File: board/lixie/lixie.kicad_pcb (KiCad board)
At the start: 2 copper layers, 1 part

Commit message: made some footprints, fixed the power diode circuitry
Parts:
- removed REF**: QFP_64, lixie:STM32L073RZT3
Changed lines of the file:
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@@
     (tracks 0)
     (zones 0)
-    (modules 1)
+    (modules 0)
     (nets 1)
   )
@@
     (uvia_drill 0.1)
   )
-  (module lixie:STM32L073RZT3 (layer F.Cu)
-    (at 154.3 95.3)
-    (fp_text reference REF** (at 0 -7.55) (layer F.SilkS)
-      (effects (font (size 1.2 1.2) (thickness 0.15)))
-    )
-    (fp_text value QFP_64 (at 0 7.55) (layer F.Fab)
-      (effects (font (size 1.2 1.2) (thickness 0.15)))
-    )
-    (fp_line (start -5 -4.25) (end -4.25 -5) (layer F.SilkS) (width 0.15))
-    (fp_line (start 4.25 -5) (end 5 -5) (layer F.SilkS) (width 0.15))
-    (fp_line (start 5 -5) (end 5 -4.25) (layer F.SilkS) (width 0.15))
-    (fp_line (start -4.25 5) (end -5 5) (layer F.SilkS) (width 0.15))
-    (fp_line (start -5 5) (end -5 4.25) (layer F.SilkS) (width 0.15))
-    (fp_line (start 4.25 5) (end 5 5) (layer F.SilkS) (width 0.15))
-    (fp_line (start 5 5) (end 5 4.25) (layer F.SilkS) (width 0.15))
-    (fp_line (start -6.6 -6.6) (end 6.6 -6.6) (layer F.CrtYd) (width 0.15))
-    (fp_line (start 6.6 -6.6) (end 6.6 6.6) (layer F.CrtYd) (width 0.15))
-    (fp_line (start 6.6 6.6) (end -6.6 6.6) (layer F.CrtYd) (width 0.15))
-    (fp_line (start -6.6 6.6) (end -6.6 -6.6) (layer F.CrtYd) (width 0.15))
-    (pad 1 smd oval (at -5.75 -3.75 90) (size 0.3 1.2) (layers F.Cu F.Paste F.Mask)
-      (solder_mask_margin 0.001))
-    (pad 2 smd oval (at -5.75 -3.25 90) (size 0.3 1.2) (layers F.Cu F.Paste F.Mask)
-      (solder_mask_margin 0.0001))
-    (pad 3 smd oval (at -5.75 -2.75 90) (size 0.3 1.2) (layers F.Cu F.Paste F.Mask)
-      (solder_mask_margin 0.000001))
-    (pad 4 smd oval (at -5.75 -2.25 90) (size 0.3 1.2) (layers F.Cu F.Paste F.Mask)
-      (solder_mask_margin 0.000001))
-    (pad 5 smd oval (at -5.75 -1.75 90) (size 0.3 1.2) (layers F.Cu F.Paste F.Mask)
-      (solder_mask_margin 0.000001))
-    (pad 6 smd oval (at -5.75 -1.25 90) (size 0.3 1.2) (layers F.Cu F.Paste F.Mask)
-      (solder_mask_margin 0.000001))
-    (pad 7 smd oval (at -5.75 -0.75 90) (size 0.3 1.2) (layers F.Cu F.Paste F.Mask)
-      (solder_mask_margin 0.000001))
-    (pad 8 smd oval (at -5.75 -0.25 90) (size 0.3 1.2) (layers F.Cu F.Paste F.Mask)
-      (solder_mask_margin 0.000001))
-    (pad 9 smd oval (at -5.75 0.25 90) (size 0.3 1.2) (layers F.Cu F.Paste F.Mask)
-      (solder_mask_margin 0.000001))
-    (pad 10 smd oval (at -5.75 0.75 270) (size 0.3 1.2) (layers F.Cu F.Paste F.Mask)
-      (solder_mask_margin 0.000001))
-    (pad 11 smd oval (at -5.75 1.25 270) (size 0.3 1.2) (layers F.Cu F.Paste F.Mask)
-      (solder_mask_margin 0.000001))
-    (pad 12 smd oval (at -5.75 1.75 90) (size 0.3 1.2) (layers F.Cu F.Paste F.Mask)
-      (solder_mask_margin 0.000001))
-    (pad 13 smd oval (at -5.75 2.25 270) (size 0.3 1.2) (layers F.Cu F.Paste F.Mask)
-      (solder_mask_margin 0.000001))
-    (pad 14 smd oval (at -5.75 2.75 90) (size 0.3 1.2) (layers F.Cu F.Paste F.Mask)
-      (solder_mask_margin 0.000001))
-    (pad 15 smd oval (at -5.75 3.25 90) (size 0.3 1.2) (layers F.Cu F.Paste F.Mask)
-      (solder_mask_margin 0.000001))
-    (pad 16 smd oval (at -5.75 3.75 90) (size 0.3 1.2) (layers F.Cu F.Paste F.Mask)
-      (solder_mask_margin 0.000001))
-    (pad 17 smd oval (at -3.75 5.75) (size 0.3 1.2) (layers F.Cu F.Paste F.Mask)
-      (solder_mask_margin 0.000001))
-    (pad 18 smd oval (at -3.25 5.75) (size 0.3 1.2) (layers F.Cu F.Paste F.Mask)
-      (solder_mask_margin 0.000001))
-    (pad 19 smd oval (at -2.75 5.75) (size 0.3 1.2) (layers F.Cu F.Paste F.Mask)
-      (solder_mask_margin 0.000001))
-    (pad 20 smd oval (at -2.25 5.75) (size 0.3 1.2) (layers F.Cu F.Paste F.Mask)
-      (solder_mask_margin 0.000001))
-    (pad 21 smd oval (at -1.75 5.75) (size 0.3 1.2) (layers F.Cu F.Paste F.Mask)
-      (solder_mask_margin 0.000001))
-    (pad 22 smd oval (at -1.25 5.75) (size 0.3 1.2) (layers F.Cu F.Paste F.Mask)
-      (solder_mask_margin 0.000001))
-    (pad 23 smd oval (at -0.75 5.75) (size 0.3 1.2) (layers F.Cu F.Paste F.Mask)
-      (solder_mask_margin 0.000001))
-    (pad 24 smd oval (at -0.25 5.75) (size 0.3 1.2) (layers F.Cu F.Paste F.Mask)
-      (solder_mask_margin 0.000001))
-    (pad 25 smd oval (at 0.25 5.75) (size 0.3 1.2) (layers F.Cu F.Paste F.Mask)
-      (solder_mask_margin 0.000001))
-    (pad 26 smd oval (at 0.75 5.75) (size 0.3 1.2) (layers F.Cu F.Paste F.Mask)
-      (solder_mask_margin 0.000001))
-    (pad 27 smd oval (at 1.25 5.75) (size 0.3 1.2) (layers F.Cu F.Paste F.Mask)
-      (solder_mask_margin 0.000001))
-    (pad 28 smd oval (at 1.75 5.75) (size 0.3 1.2) (layers F.Cu F.Paste F.Mask)
-      (solder_mask_margin 0.000001))
-    (pad 29 smd oval (at 2.25 5.75) (size 0.3 1.2) (layers F.Cu F.Paste F.Mask)
-      (solder_mask_margin 0.000001))
-    (pad 30 smd oval (at 2.75 5.75) (size 0.3 1.2) (layers F.Cu F.Paste F.Mask)
-      (solder_mask_margin 0.000001))
-    (pad 31 smd oval (at 3.25 5.75) (size 0.3 1.2) (layers F.Cu F.Paste F.Mask)
-      (solder_mask_margin 0.000001))
-    (pad 32 smd oval (at 3.75 5.75) (size 0.3 1.2) (layers F.Cu F.Paste F.Mask)
-      (solder_mask_margin 0.000001))
-    (pad 33 smd oval (at 5.75 3.75 90) (size 0.3 1.2) (layers F.Cu F.Paste F.Mask)
-      (solder_mask_margin 0.000001))
-    (pad 34 smd oval (at 5.75 3.25 90) (size 0.3 1.2) (layers F.Cu F.Paste F.Mask)
-      (solder_mask_margin 0.000001))
-    (pad 35 smd oval (at 5.75 2.75 90) (size 0.3 1.2) (layers F.Cu F.Paste F.Mask)
-      (solder_mask_margin 0.000001))
-    (pad 36 smd oval (at 5.75 2.25 90) (size 0.3 1.2) (layers F.Cu F.Paste F.Mask)
-      (solder_mask_margin 0.000001))
-    (pad 37 smd oval (at 5.75 1.75 90) (size 0.3 1.2) (layers F.Cu F.Paste F.Mask)
-      (solder_mask_margin 0.000001))
-    (pad 38 smd oval (at 5.75 1.25 90) (size 0.3 1.2) (layers F.Cu F.Paste F.Mask)
-      (solder_mask_margin 0.000001))
-    (pad 39 smd oval (at 5.75 0.75 90) (size 0.3 1.2) (layers F.Cu F.Paste F.Mask)
-      (solder_mask_margin 0.000001))
-    (pad 40 smd oval (at 5.75 0.25 90) (size 0.3 1.2) (layers F.Cu F.Paste F.Mask)
-      (solder_mask_margin 0.000001))
-    (pad 41 smd oval (at 5.75 -0.25 90) (size 0.3 1.2) (layers F.Cu F.Paste F.Mask)
-      (solder_mask_margin 0.000001))
-    (pad 42 smd oval (at 5.75 -0.75 90) (size 0.3 1.2) (layers F.Cu F.Paste F.Mask)
-      (solder_mask_margin 0.000001))
-    (pad 43 smd oval (at 5.75 -1.25 90) (size 0.3 1.2) (layers F.Cu F.Paste F.Mask)
-      (solder_mask_margin 0.000001))
-    (pad 44 smd oval (at 5.75 -1.75 90) (size 0.3 1.2) (layers F.Cu F.Paste F.Mask)
-      (solder_mask_margin 0.000001))
-    (pad 45 smd oval (at 5.75 -2.25 90) (size 0.3 1.2) (layers F.Cu F.Paste F.Mask)
-      (solder_mask_margin 0.000001))
-    (pad 46 smd oval (at 5.75 -2.75 90) (size 0.3 1.2) (layers F.Cu F.Paste F.Mask)
-      (solder_mask_margin 0.000001))
-    (pad 47 smd oval (at 5.75 -3.25 90) (size 0.3 1.2) (layers F.Cu F.Paste F.Mask)
-      (solder_mask_margin 0.000001))
-    (pad 48 smd oval (at 5.75 -3.75 90) (size 0.3 1.2) (layers F.Cu F.Paste F.Mask)
-      (solder_mask_margin 0.000001))
-    (pad 49 smd oval (at 3.75 -5.75) (size 0.3 1.2) (layers F.Cu F.Paste F.Mask)
-      (solder_mask_margin 0.000001))
-    (pad 50 smd oval (at 3.25 -5.75) (size 0.3 1.2) (layers F.Cu F.Paste F.Mask)
-      (solder_mask_margin 0.000001))
-    (pad 51 smd oval (at 2.75 -5.75) (size 0.3 1.2) (layers F.Cu F.Paste F.Mask)
-      (solder_mask_margin 0.000001))
-    (pad 52 smd oval (at 2.25 -5.75) (size 0.3 1.2) (layers F.Cu F.Paste F.Mask)
-      (solder_mask_margin 0.000001))
-    (pad 53 smd oval (at 1.75 -5.75) (size 0.3 1.2) (layers F.Cu F.Paste F.Mask)
-      (solder_mask_margin 0.000001))
-    (pad 54 smd oval (at 1.25 -5.75) (size 0.3 1.2) (layers F.Cu F.Paste F.Mask)
-      (solder_mask_margin 0.000001))
-    (pad 55 smd oval (at 0.75 -5.75) (size 0.3 1.2) (layers F.Cu F.Paste F.Mask)
-      (solder_mask_margin 0.000001))
-    (pad 56 smd oval (at 0.25 -5.75) (size 0.3 1.2) (layers F.Cu F.Paste F.Mask)
-      (solder_mask_margin 0.000001))
-    (pad 57 smd oval (at -0.25 -5.75) (size 0.3 1.2) (layers F.Cu F.Paste F.Mask)
-      (solder_mask_margin 0.000001))
-    (pad 58 smd oval (at -0.75 -5.75) (size 0.3 1.2) (layers F.Cu F.Paste F.Mask)
-      (solder_mask_margin 0.000001))
-    (pad 59 smd oval (at -1.25 -5.75) (size 0.3 1.2) (layers F.Cu F.Paste F.Mask)
-      (solder_mask_margin 0.000001))
-    (pad 60 smd oval (at -1.75 -5.75) (size 0.3 1.2) (layers F.Cu F.Paste F.Mask)
-      (solder_mask_margin 0.000001))
-    (pad 61 smd oval (at -2.25 -5.75) (size 0.3 1.2) (layers F.Cu F.Paste F.Mask)
-      (solder_mask_margin 0.000001))
-    (pad 62 smd oval (at -2.75 -5.75) (size 0.3 1.2) (layers F.Cu F.Paste F.Mask)
-      (solder_mask_margin 0.000001))
-    (pad 63 smd oval (at -3.25 -5.75) (size 0.3 1.2) (layers F.Cu F.Paste F.Mask)
-      (solder_mask_margin 0.000001))
-    (pad 64 smd oval (at -3.75 -5.75) (size 0.3 1.2) (layers F.Cu F.Paste F.Mask)
-      (solder_mask_margin 0.000001))
-  )
 )

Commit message: started working on layout
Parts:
- added BT1: Battery_Cell, Pin_Headers:Pin_Header_Straight_1x02, F.Cu at (82.0, 75.5)
- added D1: LED_ARGB, lixie:LED_ARGB_0606, F.Cu at (93.0, 89.0)
- added D10: LED_ARGB, lixie:LED_ARGB_0606, F.Cu at (103.0, 83.0)
- added D11: LED_ARGB, lixie:LED_ARGB_0606, F.Cu at (113.0, 83.0)
- added D12: LED_ARGB, lixie:LED_ARGB_0606, F.Cu at (123.0, 83.0)
- added D13: LED_ARGB, lixie:LED_ARGB_0606, F.Cu at (98.0, 80.0)
- added D14: LED_ARGB, lixie:LED_ARGB_0606, F.Cu at (108.0, 80.0)
- added D15: LED_ARGB, lixie:LED_ARGB_0606, F.Cu at (118.2, 80.0)
- added D16: LED_ARGB, lixie:LED_ARGB_0606, F.Cu at (128.0, 80.0)
- added D17: D, Diodes_SMD:SOD-123, F.Cu at (85.8, 62.0)
- added D2: LED_ARGB, lixie:LED_ARGB_0606, F.Cu at (103.0, 89.0)
- added D3: LED_ARGB, lixie:LED_ARGB_0606, F.Cu at (113.0, 89.0)
- added D4: LED_ARGB, lixie:LED_ARGB_0606, F.Cu at (123.0, 89.0)
- added D5: LED_ARGB, lixie:LED_ARGB_0606, F.Cu at (98.0, 86.0)
- added D6: LED_ARGB, lixie:LED_ARGB_0606, F.Cu at (108.0, 86.0)
- added D7: LED_ARGB, lixie:LED_ARGB_0606, F.Cu at (118.2, 86.0)
- added D8: LED_ARGB, lixie:LED_ARGB_0606, F.Cu at (128.0, 86.0)
- added D9: LED_ARGB, lixie:LED_ARGB_0606, F.Cu at (93.0, 83.0)
- added LS1: Speaker, lixie:PKMCS0909E4000-R1, F.Cu at (111.5, 63.8)
- added P1: USB_OTG, lixie:USB_Micro-B_Molex-105017-0001, F.Cu at (142.0, 73.0)
- added R1: 100k, Resistors_SMD:R_0805_HandSoldering, F.Cu at (87.0, 67.5)
- added R2: 100k, Resistors_SMD:R_0805_HandSoldering, F.Cu at (90.0, 67.5)
- added R3: 100k, Resistors_SMD:R_0805_HandSoldering, F.Cu at (93.0, 67.5)
- added R4: 10k, Resistors_SMD:R_0805_HandSoldering, F.Cu at (136.8, 62.8)
- added R5: R, Resistors_SMD:R_0805_HandSoldering, F.Cu at (136.7, 68.8)
- added U1: IS31FL3738, lixie:IS31FL3738, F.Cu at (101.0, 66.2)
- added U2: MIC550x, lixie:MIC550x, F.Cu at (95.2, 61.8)
- added U3: MAX40200, lixie:MAX40200, F.Cu at (90.0, 61.8)
- added U4: STM32L073xZ, lixie:STM32L073RZT3, F.Cu at (127.8, 65.8)
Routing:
- net Net-(D10-Pad2): track 0.00 -> 60.6 mm, vias 0 -> 8
- net Net-(D10-Pad4): track 0.00 -> 53.7 mm
- net Net-(D1-Pad4): track 0.00 -> 49.5 mm
- net Net-(D1-Pad3): track 0.00 -> 47.9 mm
- net Net-(D10-Pad3): track 0.00 -> 46.0 mm
- net Net-(D1-Pad2): track 0.00 -> 37.5 mm, vias 0 -> 5
- net VBUS: track 0.00 -> 14.4 mm
- net Net-(D7-Pad2): track 0.00 -> 12.0 mm, vias 0 -> 2
- net Net-(D12-Pad1): track 0.00 -> 6.82 mm, vias 0 -> 2
- net Net-(D16-Pad1): track 0.00 -> 6.82 mm, vias 0 -> 2
- net Net-(D14-Pad1): track 0.00 -> 6.82 mm, vias 0 -> 2
- net Net-(D13-Pad1): track 0.00 -> 6.82 mm, vias 0 -> 2
- net Net-(D1-Pad1): track 0.00 -> 6.75 mm, vias 0 -> 2
- net Net-(D11-Pad1): track 0.00 -> 6.68 mm, vias 0 -> 2
- net Net-(D15-Pad1): track 0.00 -> 6.59 mm, vias 0 -> 2
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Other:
- board outline added: 67.5 x 37.8 mm

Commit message: laid out the board
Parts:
- removed LS1: Speaker, lixie:PKMCS0909E4000-R1
- added F1: Polyfuse, Resistors_SMD:R_1206_HandSoldering, F.Cu at (74.2, 77.3)
- added F2: Polyfuse, Resistors_SMD:R_1206_HandSoldering, F.Cu at (84.3, 75.4)
- added F3: Polyfuse, Resistors_SMD:R_1206_HandSoldering, F.Cu at (130.0, 73.0)
- added R6: 4.7k, Resistors_SMD:R_0805_HandSoldering, F.Cu at (102.2, 65.8)
- added SLEEP: SW_Push, Buttons_Switches_SMD:SW_SPST_TL3342, F.Cu at (80.6, 66.9)
- added SWD: CONN_01X04, Pin_Headers:Pin_Header_Straight_1x04, F.Cu at (119.8, 80.4)
- D1, D10, D11, D12, D13, D14, D15, D16, D2, D3, D4, D5, D6, D7, D8, D9: value LED_ARGB -> LED_RGAB
- R5: value R -> 4.7k
- moved R5 32.6 mm to (104.3, 65.8)
- moved D17 17.4 mm to (73.2, 74.0), turned to 180 degrees
- moved U3 16.8 mm to (78.2, 73.7), turned to 0 degrees
- moved U2 16.3 mm to (82.6, 72.1), turned to 90 degrees
- moved R3 11.9 mm to (103.7, 72.6)
- moved BT1 8.96 mm to (74.6, 80.6), turned to 270 degrees
- moved D1 8.06 mm to (86.0, 93.0)
- moved D10 8.06 mm to (96.0, 87.0)
- moved D11 8.06 mm to (106.0, 87.0)
- moved D12 8.06 mm to (116.0, 87.0)
- moved D13 8.06 mm to (91.0, 84.0)
- moved D14 8.06 mm to (101.0, 84.0)
- moved D15 8.06 mm to (111.2, 84.0)
- moved D16 8.06 mm to (121.0, 84.0)
- moved D2 8.06 mm to (96.0, 93.0)
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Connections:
- net Net-(R3-Pad1) renamed /LED_CURRENT
- D11 pad 1: Net-(D11-Pad1) -> Net-(D10-Pad1)
- D11 pad 3: Net-(D10-Pad3) -> Net-(D11-Pad3)
- D12 pad 1: Net-(D12-Pad1) -> Net-(D10-Pad1)
- D12 pad 3: Net-(D10-Pad3) -> Net-(D12-Pad3)
- D13 pad 1: Net-(D13-Pad1) -> Net-(D10-Pad1)
- D13 pad 3: Net-(D10-Pad3) -> Net-(D13-Pad3)
- D14 pad 1: Net-(D14-Pad1) -> Net-(D10-Pad1)
- D14 pad 3: Net-(D10-Pad3) -> Net-(D14-Pad3)
- D15 pad 1: Net-(D15-Pad1) -> Net-(D10-Pad1)
- D15 pad 3: Net-(D10-Pad3) -> Net-(D15-Pad3)
- D16 pad 1: Net-(D16-Pad1) -> Net-(D10-Pad1)
- D16 pad 3: Net-(D10-Pad3) -> Net-(D16-Pad3)
- D17 pad 1: VBUS -> Net-(D17-Pad1)
- D17 pad 2: +5V -> Net-(D17-Pad2)
- D2 pad 1: Net-(D10-Pad1) -> Net-(D1-Pad1)
- D2 pad 3: Net-(D1-Pad3) -> Net-(D10-Pad3)
- D3 pad 1: Net-(D11-Pad1) -> Net-(D1-Pad1)
- D3 pad 3: Net-(D1-Pad3) -> Net-(D11-Pad3)
- D4 pad 1: Net-(D12-Pad1) -> Net-(D1-Pad1)
- D4 pad 3: Net-(D1-Pad3) -> Net-(D12-Pad3)
- D5 pad 1: Net-(D13-Pad1) -> Net-(D1-Pad1)
- D5 pad 3: Net-(D1-Pad3) -> Net-(D13-Pad3)
- D6 pad 1: Net-(D14-Pad1) -> Net-(D1-Pad1)
- D6 pad 3: Net-(D1-Pad3) -> Net-(D14-Pad3)
- D7 pad 1: Net-(D15-Pad1) -> Net-(D1-Pad1)
- D7 pad 2: Net-(D7-Pad2) -> Net-(D1-Pad2)
- D7 pad 3: Net-(D1-Pad3) -> Net-(D15-Pad3)
- D8 pad 1: Net-(D16-Pad1) -> Net-(D1-Pad1)
- D8 pad 2: Net-(D7-Pad2) -> Net-(D1-Pad2)
- D8 pad 3: Net-(D1-Pad3) -> Net-(D16-Pad3)
- D9 pad 1: Net-(D1-Pad1) -> Net-(D10-Pad1)
- D9 pad 3: Net-(D10-Pad3) -> Net-(D1-Pad3)
- R5 pad 1: /PIEZO -> +3V3
- R5 pad 2: Net-(LS1-Pad2) -> /SDA
- U1 pad 10: Net-(D1-Pad1) -> Net-(D1-Pad3)
- U1 pad 11: Net-(D10-Pad1) -> Net-(D10-Pad3)
- U1 pad 13: Net-(D11-Pad1) -> Net-(D11-Pad3)
- U1 pad 14: Net-(D12-Pad1) -> Net-(D12-Pad3)
- U1 pad 15: Net-(D13-Pad1) -> Net-(D13-Pad3)
- U1 pad 16: Net-(D14-Pad1) -> Net-(D14-Pad3)
- U1 pad 18: Net-(D15-Pad1) -> Net-(D15-Pad3)
- U1 pad 19: Net-(D16-Pad1) -> Net-(D16-Pad3)
- U1 pad 3: Net-(D10-Pad3) -> Net-(D10-Pad2)
- U1 pad 5: Net-(D10-Pad2) -> Net-(D10-Pad1)
- U1 pad 7: Net-(D1-Pad3) -> Net-(D1-Pad2)
- U1 pad 9: Net-(D1-Pad2) -> Net-(D1-Pad1)
- U3 pad 1: +BATT -> Net-(F1-Pad1)
- U3 pad 3: +BATT -> Net-(F1-Pad1)
- U3 pad 5: VBUS -> Net-(D17-Pad1)
- U4 pad 2: /BTN_SLEEP -> Net-(SW1-Pad2)
- U4 pad 46: /DBG_TMS -> /SWDIO
- U4 pad 49: /DBG_TCK -> /SWCLK
- U4 pad 53: /PIEZO -> Net-(U4-Pad53)
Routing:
- net +3V3: track 0.00 -> 98.8 mm, vias 0 -> 2
- net Net-(D17-Pad2): track 0.00 -> 93.7 mm, vias 0 -> 2
- net Net-(D1-Pad1): track 6.75 -> 75.4 mm, vias 2 -> 0
- net Net-(D10-Pad1): track 6.59 -> 64.7 mm
- net GND: track 0.00 -> 57.9 mm, vias 0 -> 15
- net Net-(SW1-Pad2): track 0.00 -> 50.5 mm
- net Net-(D1-Pad2): track 37.5 -> 87.8 mm, vias 5 -> 12
- net Net-(D1-Pad4): track 49.5 -> 95.0 mm, vias 0 -> 2
- net VBUS: track 14.4 -> 57.0 mm, vias 0 -> 5
- net Net-(D10-Pad4): track 53.7 -> 95.3 mm, vias 0 -> 4
- net Net-(D16-Pad3): track 0.00 -> 39.1 mm, vias 0 -> 3
- net Net-(D12-Pad3): track 0.00 -> 35.4 mm, vias 0 -> 3
- net Net-(D15-Pad3): track 0.00 -> 35.0 mm, vias 0 -> 3
- net /SDA: track 0.00 -> 32.0 mm, vias 0 -> 2
- net /SCL: track 0.00 -> 30.8 mm, vias 0 -> 2
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- added copper zone on B.Cu, net GND
- added copper zone on F.Cu, net GND
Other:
- net class Default: clearance 0.2 -> 0.19999
- rule trace_clearance: 0.2 -> 0.19999
- board text added: "-"
- board text added: "CLK"
- board text added: "G"
- board text added: "IO"
- board text added: "V"

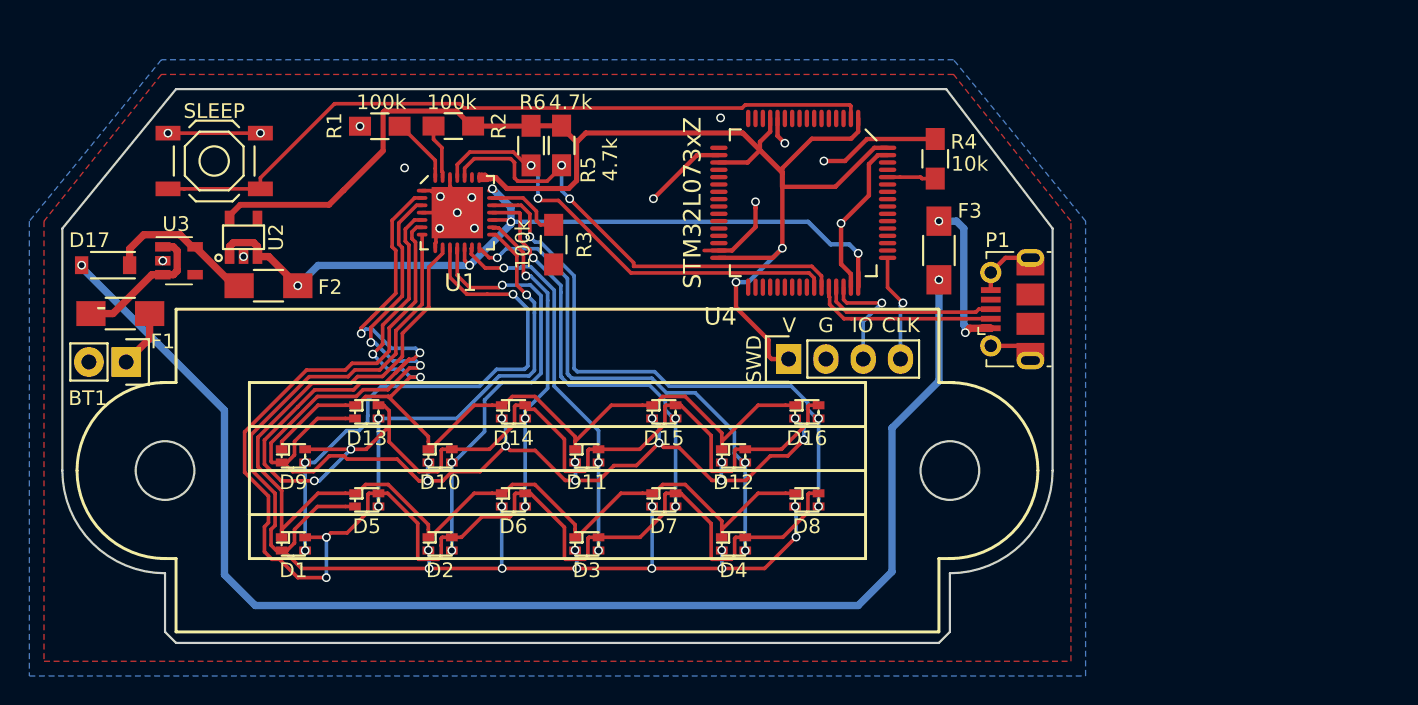
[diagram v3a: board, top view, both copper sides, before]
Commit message: added some test points
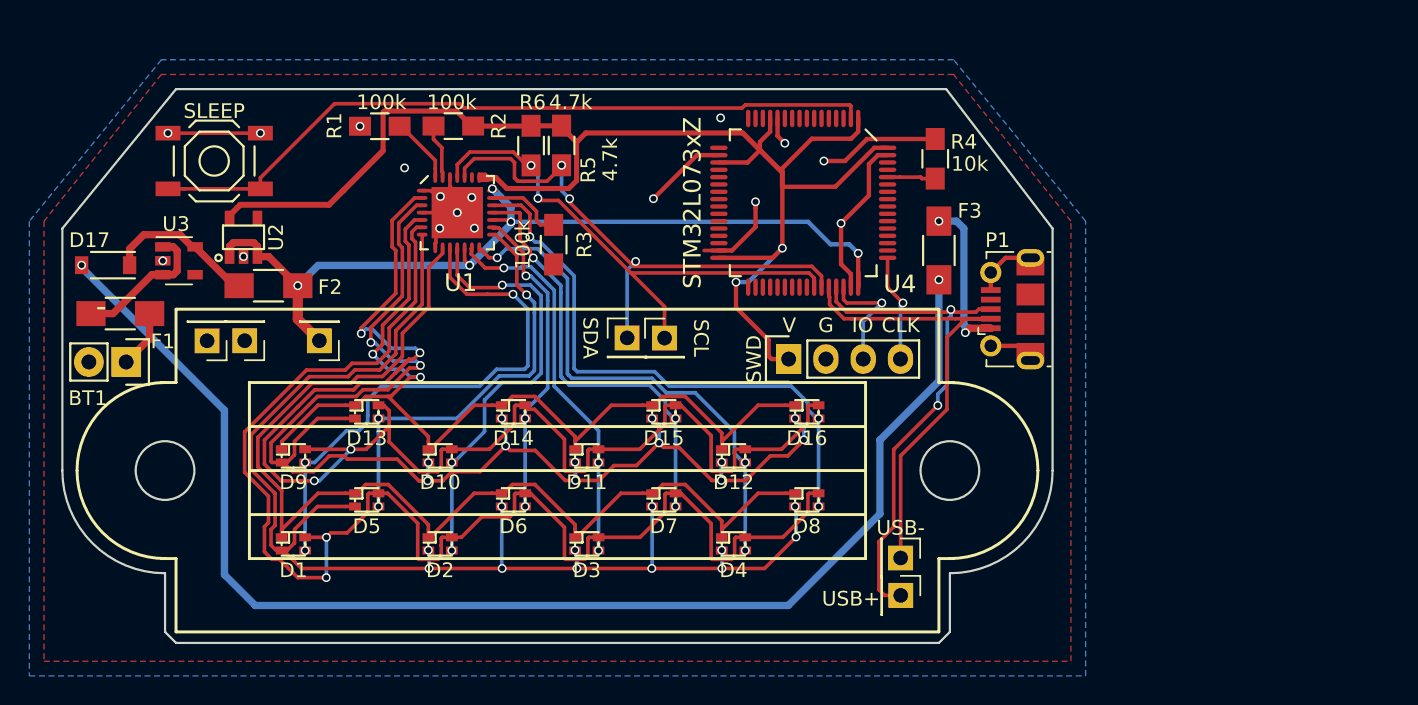
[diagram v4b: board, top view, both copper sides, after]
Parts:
- added SCL_TST1: TestPoint, Connector_PinHeader_2.54mm:PinHeader_1x01_P2.54mm_Vertical, F.Cu at (111.3, 79.0)
- added SDA_TST1: TestPoint, Connector_PinHeader_2.54mm:PinHeader_1x01_P2.54mm_Vertical, F.Cu at (108.8, 79.0)
- added USB_DM_TST1: TestPoint, Connector_PinHeader_2.54mm:PinHeader_1x01_P2.54mm_Vertical, F.Cu at (127.4, 94.0)
- added USB_DP_GND1: TestPoint, Connector_PinHeader_2.54mm:PinHeader_1x01_P2.54mm_Vertical, F.Cu at (82.7, 79.2)
- added USB_DP_GND2: TestPoint, Connector_PinHeader_2.54mm:PinHeader_1x01_P2.54mm_Vertical, F.Cu at (80.1, 79.2)
- added USB_DP_TST1: TestPoint, Connector_PinHeader_2.54mm:PinHeader_1x01_P2.54mm_Vertical, F.Cu at (127.4, 96.5)
- added VBUS_TST1: TestPoint, Connector_PinHeader_2.54mm:PinHeader_1x01_P2.54mm_Vertical, F.Cu at (87.8, 79.2)
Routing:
- net /USB_DP: track 11.9 -> 34.9 mm, vias 0 -> 2
- net /USB_DM: track 12.6 -> 32.4 mm
- net /SDA: track 32.0 -> 37.9 mm, vias 2 -> 3
- net /SCL: track 30.8 -> 36.2 mm
- net VBUS: track 57.0 -> 61.3 mm
- net Net-(D17-Pad2): track 93.7 -> 90.9 mm
- net GND: vias 15 -> 17
- net (no net): vias 2 -> 0
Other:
- board text added: "SCL"
- board text added: "SDA"
- board text added: "USB+"
- board text added: "USB-"
